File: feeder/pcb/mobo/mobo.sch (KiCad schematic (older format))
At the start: 63 parts, among them J1 FTDI_HEADER, J2 PLATED_PADS, J3 SWD_10, M1 DRIVE_MOTOR, M2 PEEL_MOTOR, SW1 BUTTON_1, SW2 BUTTON_2, SW3 RESET, U1 TCS40DPR, U2 VCNT2020, U3 MAX3078E, U4 DRV8833PWP, U5 AP1117-33, U6 STM32F103C8Tx, U7 MCP16301, U8 QRE1113, Y1 8MHz

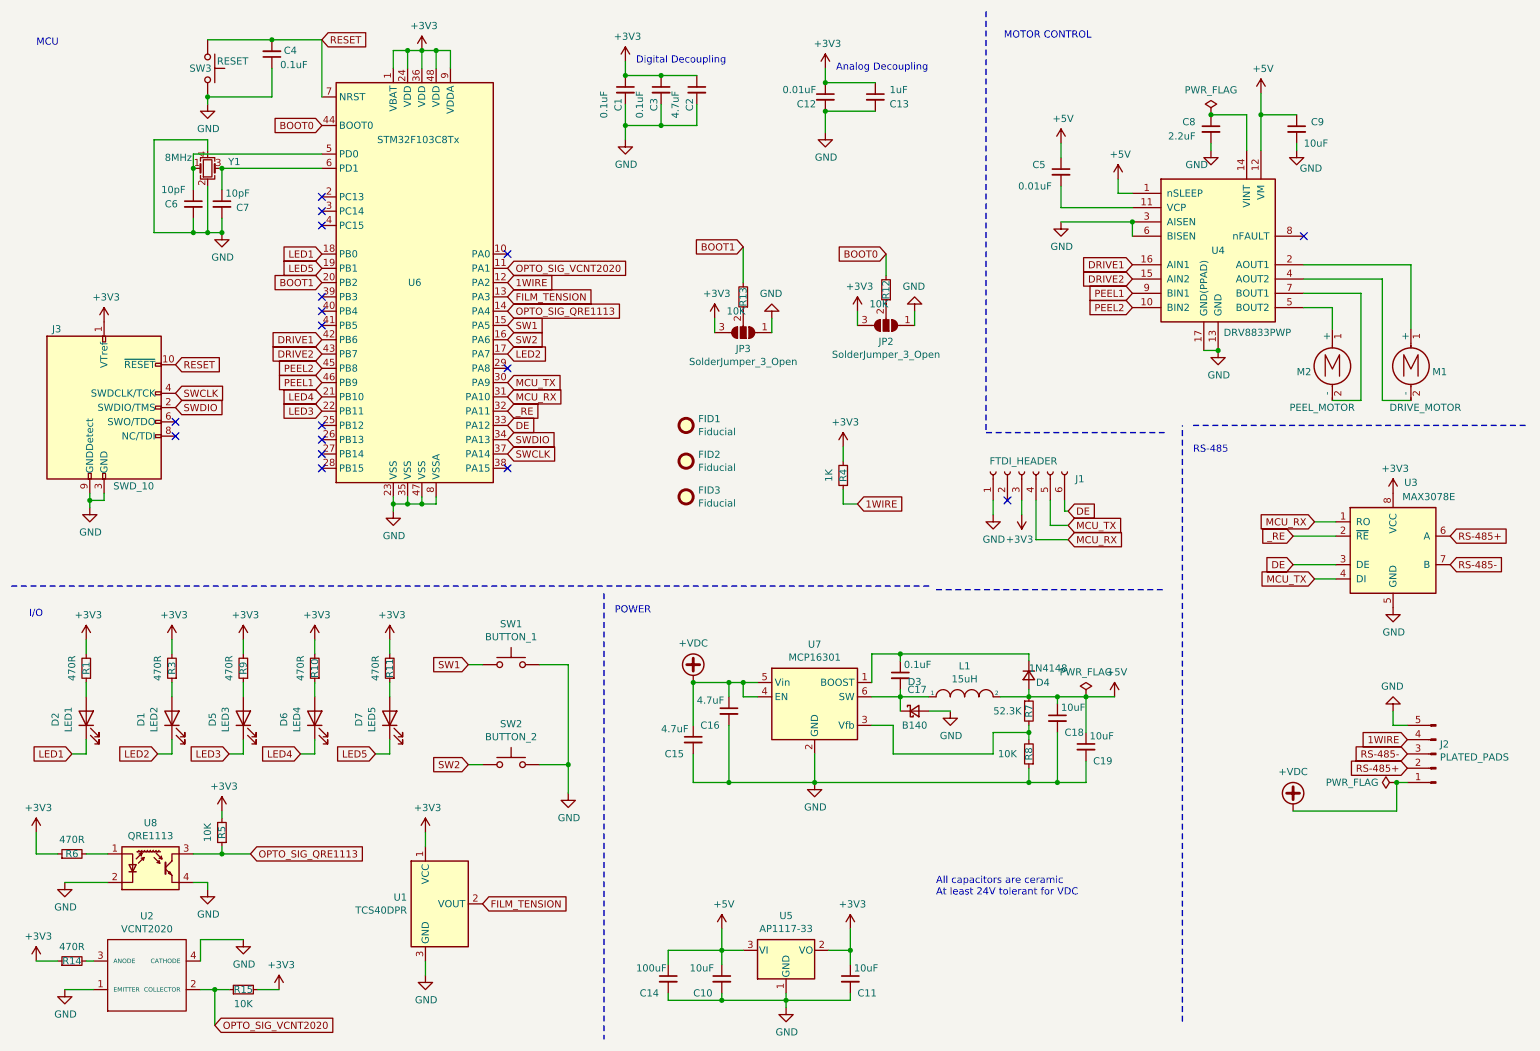
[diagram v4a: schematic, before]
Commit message: Cleanup Feeders and beautify them
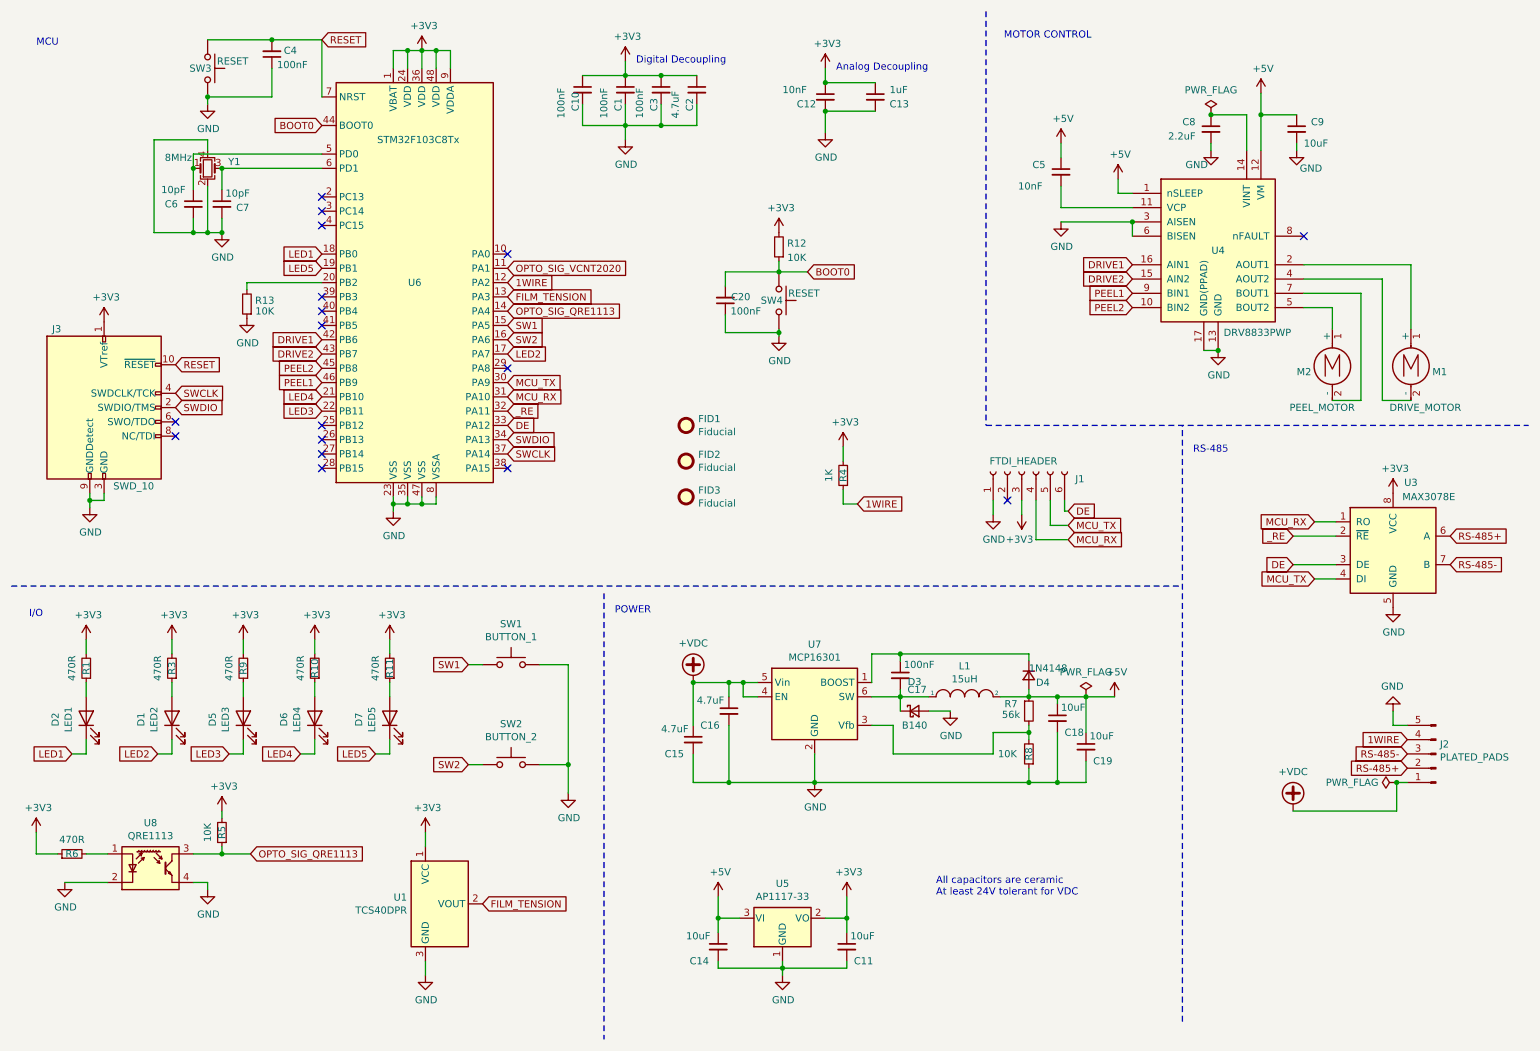
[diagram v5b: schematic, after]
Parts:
- removed JP2, JP3: SolderJumper_3_Open, Jumper:SolderJumper-3_P1.3mm_Open_RoundedPad1.0x1.5mm, symbol Jumper:SolderJumper_3_Open
- removed R14: 470R, Resistor_SMD:R_0805_2012Metric, symbol Device:R_Small
- removed R15: 10K, Resistor_SMD:R_0805_2012Metric, symbol Device:R_Small
- removed U2: VCNT2020, index:VCNT2020, symbol index:VCNT2020
- added C20: 100nF, Capacitor_SMD:C_0805_2012Metric, symbol Device:C_Small
- added SW4: RESET, Button_Switch_SMD:Panasonic_EVQPUJ_EVQPUA, symbol Switch:SW_Push
- C1, C17, C3, C4: value 0.1uF -> 100nF
- C10: value 10uF -> 100nF; JLCPCB C15850 -> C49678
- C12, C5: value 0.01uF -> 10nF
- C14: value 100uF -> 10uF; JLCPCB (none) -> C15850
- FID1, FID2, FID3: footprint Fiducial:Fiducial_1mm_Mask2mm -> Fiducial:Fiducial_0.5mm_Mask1mm
- R7: value 52.3K -> 56k; JLCPCB C17740 -> C25638
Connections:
- net +3V3: now also C10.1, R12.2
- net +5V: no longer C10.1
- net BOOT0: now also R12.1, C20.2, SW4.1; no longer R12.2
- net GND: now also R13.1, C20.1, SW4.2
- net BOOT1: no longer names the net of R13.2, U6.20 (PB2)
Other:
- moved on the sheet: C11, C14, R12, R13, U5

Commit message: Avoid using the letter p for labels
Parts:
- R5, R6, U8: Config -VCNT2020 -> (none)
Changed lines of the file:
@@
 F 3 "~" H 1000 6450 50  0001 C CNN
 F 4 "C17710" H 1000 6450 50  0001 C CNN "JLCPCB"
-F 5 "-VCNT2020" H 1000 6450 50  0001 C CNN "Config"
+F 5 "" H 1000 6450 50  0001 C CNN "Config"
 	1    1000 6450
 	0    -1   -1   0
@@
 F 3 "~" H 2050 6300 50  0001 C CNN
 F 4 "C17414" H 2050 6300 50  0001 C CNN "JLCPCB"
-F 5 "-VCNT2020" H 2050 6300 50  0001 C CNN "Config"
+F 5 "" H 2050 6300 50  0001 C CNN "Config"
 	1    2050 6300
 	-1   0    0    1
@@
 F 3 "http://www.onsemi.com/pub/Collateral/QRE1113-D.PDF" H 1550 6650 50  0001 C CNN
 F 4 "C232862" H 1550 6550 50  0001 C CNN "JLCPCB"
-F 5 "-VCNT2020" H 1550 6550 50  0001 C CNN "Config"
+F 5 "" H 1550 6550 50  0001 C CNN "Config"
 	1    1550 6550
 	1    0    0    -1

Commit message: Add buttons LCSC PN
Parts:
- SW1, SW2, SW3, SW4: LCSC (none) -> C136662
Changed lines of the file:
@@
 F 2 "Button_Switch_SMD:Panasonic_EVQPUJ_EVQPUA" H 4075 5325 50  0001 C CNN
 F 3 "" H 4075 5325 50  0001 C CNN
+F 4 "" H 4075 5125 50  0001 C CNN "JLCPCB"
+F 5 "C136662" H 4075 5125 50  0001 C CNN "LCSC"
 	1    4075 5125
 	1    0    0    -1
@@
 F 2 "Button_Switch_SMD:Panasonic_EVQPUJ_EVQPUA" H 4075 6025 50  0001 C CNN
 F 3 "" H 4075 6025 50  0001 C CNN
+F 4 "" H 4075 5825 50  0001 C CNN "JLCPCB"
+F 5 "C136662" H 4075 5825 50  0001 C CNN "LCSC"
 	1    4075 5825
 	1    0    0    -1
@@
 F 2 "Button_Switch_SMD:Panasonic_EVQPUJ_EVQPUA" H 1950 1150 50  0001 C CNN
 F 3 "" H 1950 1150 50  0001 C CNN
+F 4 "" V 1950 950 50  0001 C CNN "JLCPCB"
+F 5 "C136662" H 1950 950 50  0001 C CNN "LCSC"
 	1    1950 950
 	0    1    1    0
@@
 F 2 "Button_Switch_SMD:Panasonic_EVQPUJ_EVQPUA" H 5950 2775 50  0001 C CNN
 F 3 "" H 5950 2775 50  0001 C CNN
+F 4 "" H 5950 2575 50  0001 C CNN "JLCPCB"
+F 5 "C136662" H 5950 2575 50  0001 C CNN "LCSC"
 	1    5950 2575
 	0    1    1    0

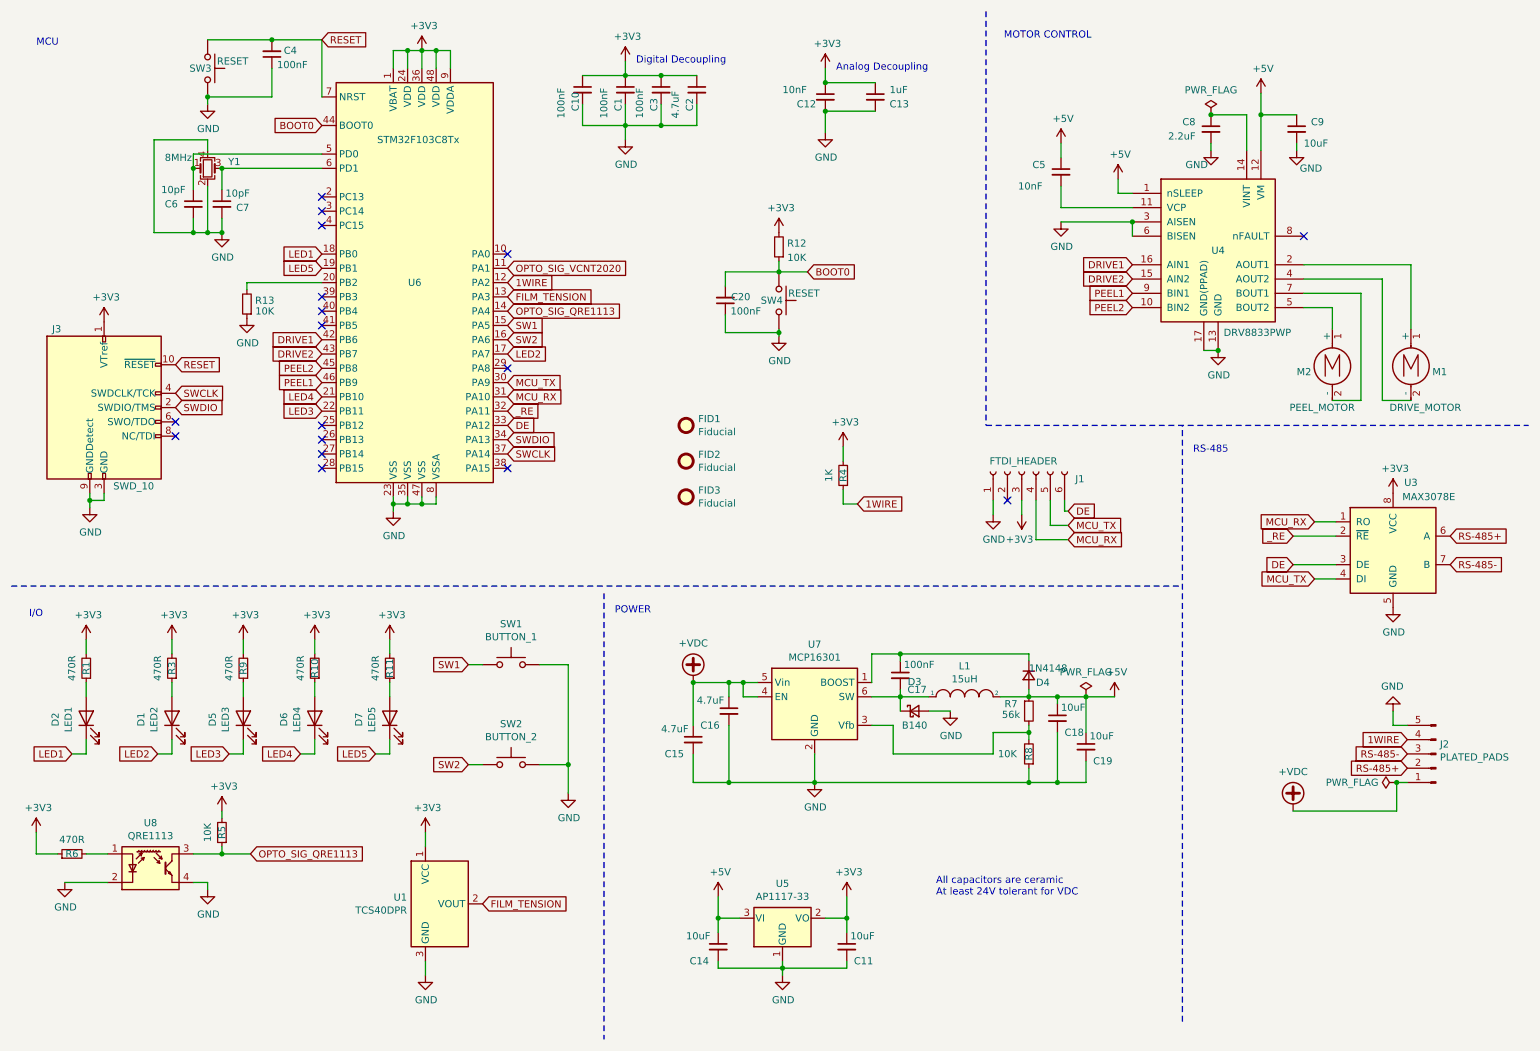
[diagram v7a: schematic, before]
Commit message: Fix reset logic level
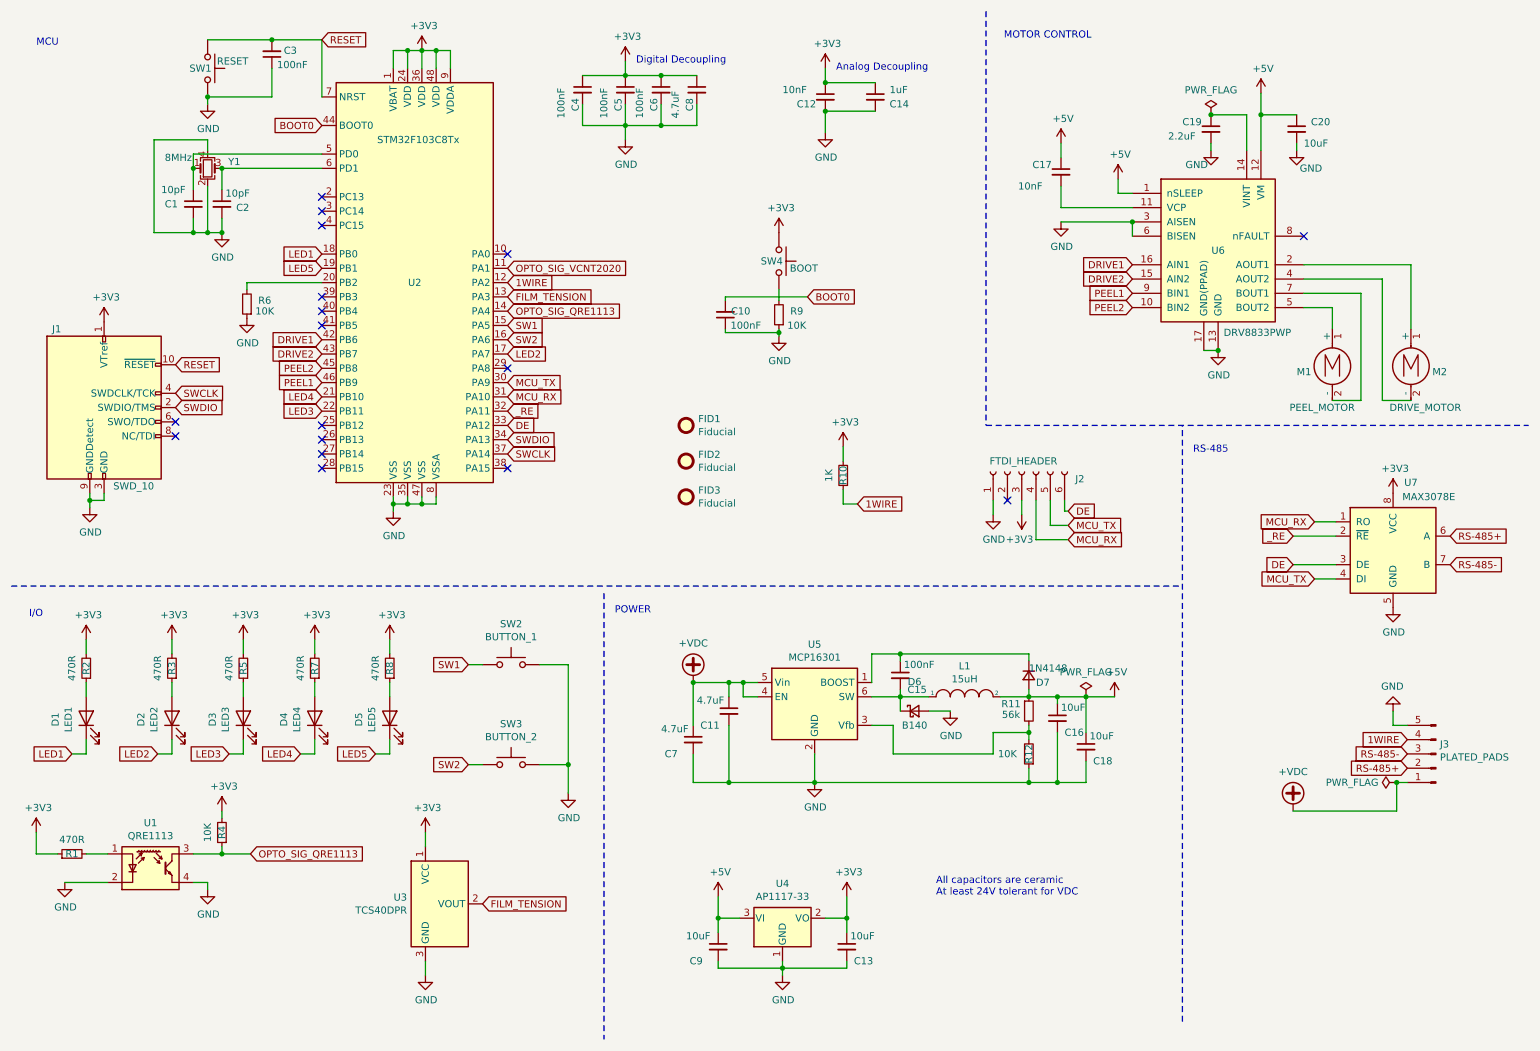
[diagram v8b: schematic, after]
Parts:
- SW4: value RESET -> BOOT
- renumbered C6 to C1, C20 to C10, C16 to C11, C11 to C13, C13 to C14, C17 to C15, C18 to C16, C5 to C17, C19 to C18, C8 to C19, C7 to C2, C9 to C20, C4 to C3, C10 to C4, C1 to C5, C3 to C6, C15 to C7, C2 to C8, C14 to C9, D2 to D1, D1 to D2, D5 to D3, D6 to D4, D7 to D5, D3 to D6, D4 to D7, J3 to J1, J1 to J2, J2 to J3, M2 to M1, M1 to M2, R6 to R1, R4 to R10, R7 to R11, R8 to R12, R1 to R2, R5 to R4, R9 to R5, R13 to R6, R10 to R7, R11 to R8, R12 to R9, SW3 to SW1, SW1 to SW2, SW2 to SW3, U8 to U1, U6 to U2, U1 to U3, U5 to U4, U7 to U5, U4 to U6, U3 to U7
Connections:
- net +3V3: now also SW4.2; no longer R9.2
- net BOOT0: no longer R9.1, SW4.1
- net GND: now also R9.1; no longer SW4.2
- new net: R9.2, SW4.1
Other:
- moved on the sheet: C10, R9, SW4
